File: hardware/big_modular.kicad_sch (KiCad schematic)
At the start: 0 parts

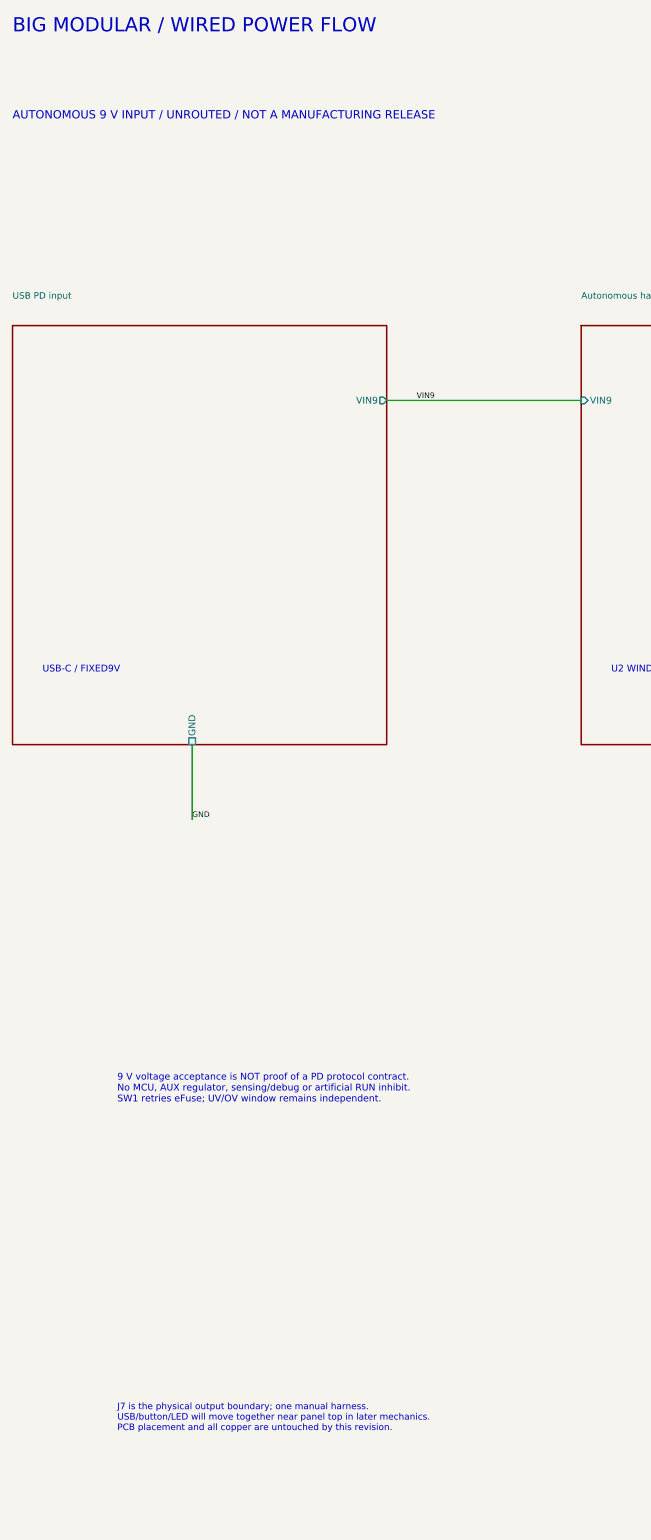
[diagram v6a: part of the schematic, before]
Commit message: Move USB, retry button and power LED to top; synchronize 64 V1 footprints without routing
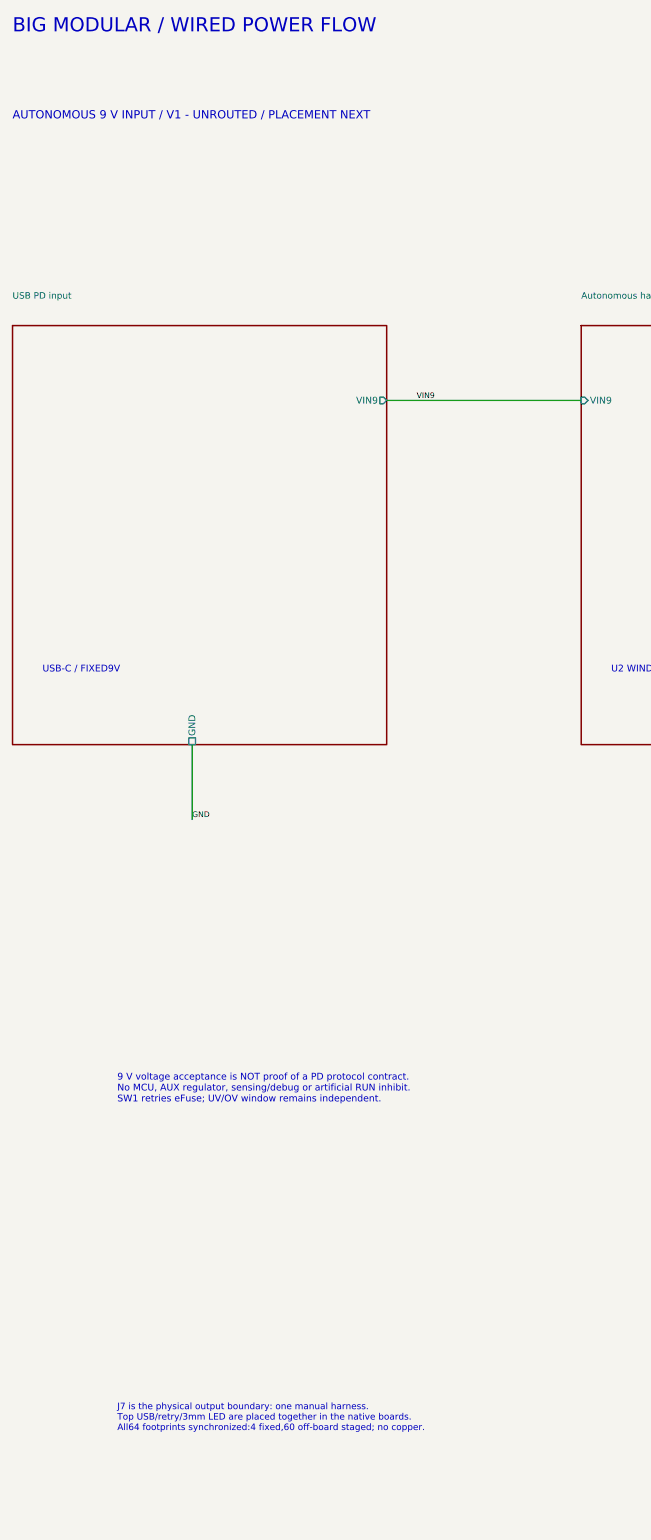
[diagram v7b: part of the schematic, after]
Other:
- note added: "AUTONOMOUS 9 V INPUT / V1 - UNROUTED / PLACEMENT NEXT"
- note added: "J7 is the physical output boundary: one manual harness. Top USB/retry/3mm LED are placed together in the native boards. All64 footprints synchronized:4 fixed,60 off-board staged; no copper."
- note removed: "AUTONOMOUS 9 V INPUT / UNROUTED / NOT A MANUFACTURING RELEASE"
- note removed: "J7 is the physical output boundary; one manual harness. USB/button/LED will move together near panel top in later mechanics. PCB placement and all copper are untouched by this revision."
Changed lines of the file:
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@@
-(kicad_sch (version 20250114) (generator "eeschema") (paper "User" 430 345)
-(title_block (title "Big Modular - V1 electrical hierarchy") (rev "V1 routing preparation") (company "Big Modular") (comment 1 "UNROUTED V1 / NOT A MANUFACTURING RELEASE"))
-(text "BIG MODULAR / WIRED POWER FLOW" (at 20.32 17.78 0) (effects (font (size 2.4 2.4)) (justify left)))
-(text "AUTONOMOUS 9 V INPUT / UNROUTED / NOT A MANUFACTURING RELEASE" (at 20.32 33.02 0) (effects (font (size 1.4 1.4)) (justify left)))
-(sheet (at 20.32 68.58) (size 63.5 71.12) (stroke (width 0.254) (type default)) (fill (color 0 0 0 0))
-(property "Sheetname" "USB PD input" (at 20.32 63.5 0) (effects (font (size 1.1 1.1)) (justify left)))
-(property "Sheetfile" "01_input_protection.kicad_sch" (at 20.32 144.78 0) (effects (font (size .85 .85)) hide))
-(pin "VIN9" output (at 83.82 81.28 0) (effects (font (size 1.15 1.15)) (justify right)))
-(pin "GND" passive (at 50.8 139.7 270) (effects (font (size 1.15 1.15)) (justify left)))
-(instances (project "big_modular" (path "/d567704c-57ad-5df1-b183-cadb01fd8972" (page "2")))) )
-(sheet (at 116.84 68.58) (size 63.5 71.12) (stroke (width 0.254) (type default)) (fill (color 0 0 0 0))
-(property "Sheetname" "Autonomous hardware window and retry" (at 116.84 63.5 0) (effects (font (size 1.1 1.1)) (justify left)))
-(property "Sheetfile" "02_hardgate.kicad_sch" (at 116.84 144.78 0) (effects (font (size .85 .85)) hide))
-(pin "VIN9" input (at 116.84 81.28 180) (effects (font (size 1.15 1.15)) (justify left)))
-(pin "VPROT" output (at 180.34 81.28 0) (effects (font (size 1.15 1.15)) (justify right)))
-(pin "GND" passive (at 147.32 139.7 270) (effects (font (size 1.15 1.15)) (justify left)))
-(instances (project "big_modular" (path "/d567704c-57ad-5df1-b183-cadb01fd8972" (page "3")))) )
-(sheet (at 213.36 68.58) (size 63.5 71.12) (stroke (width 0.254) (type default)) (fill (color 0 0 0 0))
-(property "Sheetname" "Independent buck converters" (at 213.36 63.5 0) (effects (font (size 1.1 1.1)) (justify left)))
-(property "Sheetfile" "03_bucks.kicad_sch" (at 213.36 144.78 0) (effects (font (size .85 .85)) hide))
-(pin "VPROT" input (at 213.36 81.28 180) (effects (font (size 1.15 1.15)) (justify left)))
-(pin "MID" output (at 276.86 81.28 0) (effects (font (size 1.15 1.15)) (justify right)))
-(pin "P5" output (at 276.86 111.76 0) (effects (font (size 1.15 1.15)) (justify right)))
-(pin "GND" passive (at 243.84 139.7 270) (effects (font (size 1.15 1.15)) (justify left)))
-(instances (project "big_modular" (path "/d567704c-57ad-5df1-b183-cadb01fd8972" (page "4")))) )
-(sheet (at 309.88 68.58) (size 76.2 71.12) (stroke (width 0.254) (type default)) (fill (color 0 0 0 0))
-(property "Sheetname" "Direct bipolar rails" (at 309.88 63.5 0) (effects (font (size 1.1 1.1)) (justify left)))
-(property "Sheetfile" "04_bipolar.kicad_sch" (at 309.88 144.78 0) (effects (font (size .85 .85)) hide))
-(pin "MID" input (at 309.88 81.28 180) (effects (font (size 1.15 1.15)) (justify left)))
-(pin "P12" output (at 330.2 139.7 270) (effects (font (size 1.15 1.15)) (justify left)))
-(pin "N12" output (at 360.68 139.7 270) (effects (font (size 1.15 1.15)) (justify left)))
-(pin "GND" passive (at 309.88 127.0 180) (effects (font (size 1.15 1.15)) (justify left)))
-(instances (project "big_modular" (path "/d567704c-57ad-5df1-b183-cadb01fd8972" (page "5")))) )
-(sheet (at 309.88 198.12) (size 76.2 71.12) (stroke (width 0.254) (type default)) (fill (color 0 0 0 0))
-(property "Sheetname" "Board output and power LED" (at 309.88 180.34 0) (effects (font (size 1.1 1.1)) (justify left)))
-(property "Sheetfile" "07_output_rails.kicad_sch" (at 309.88 274.32 0) (effects (font (size .85 .85)) hide))
-(pin "P12" input (at 330.2 198.12 90) (effects (font (size 1.15 1.15)) (justify right)))
-(pin "N12" input (at 360.68 198.12 90) (effects (font (size 1.15 1.15)) (justify right)))
-(pin "P5" input (at 309.88 208.28 180) (effects (font (size 1.15 1.15)) (justify left)))
-(pin "GND" passive (at 335.28 269.24 270) (effects (font (size 1.15 1.15)) (justify left)))
-(instances (project "big_modular" (path "/d567704c-57ad-5df1-b183-cadb01fd8972" (page "6")))) )
-(text "USB-C / FIXED9V" (at 25.4 127.0 0) (effects (font (size 1.15 1.15)) (justify left)))
-(text "U2 WINDOW / SW1 RETRY" (at 121.92 127.0 0) (effects (font (size 1.15 1.15)) (justify left)))
-(text "U3 MID / U5 +5V" (at 218.44 127.0 0) (effects (font (size 1.15 1.15)) (justify left)))
-(text "U4 / +/-12V" (at 314.96 127.0 0) (effects (font (size 1.15 1.15)) (justify left)))
-(text "J7 / D10 P5 LED" (at 314.96 256.54 0) (effects (font (size 1.15 1.15)) (justify left)))
-(label "GND" (at 50.8 152.4 0) (effects (font (size 0.95 0.95)) (justify left bottom)))
-(label "GND" (at 147.32 152.4 0) (effects (font (size 0.95 0.95)) (justify left bottom)))
-(label "GND" (at 243.84 152.4 0) (effects (font (size 0.95 0.95)) (justify left bottom)))
-(label "GND" (at 302.26 127.0 0) (effects (font (size 0.95 0.95)) (justify left bottom)))
-(label "GND" (at 335.28 281.94 0) (effects (font (size 0.95 0.95)) (justify left bottom)))
-(label "VIN9" (at 88.9 81.28 0) (effects (font (size 0.95 0.95)) (justify left bottom)))
-(label "VPROT" (at 185.42 81.28 0) (effects (font (size 0.95 0.95)) (justify left bottom)))
-(label "MID" (at 281.94 81.28 0) (effects (font (size 0.95 0.95)) (justify left bottom)))
-(label "P5" (at 281.94 111.76 0) (effects (font (size 0.95 0.95)) (justify left bottom)))
-(label "P12" (at 330.2 165.1 90) (effects (font (size 0.95 0.95)) (justify left bottom)))
-(label "N12" (at 360.68 165.1 90) (effects (font (size 0.95 0.95)) (justify left bottom)))
-(text "9 V voltage acceptance is NOT proof of a PD protocol contract.\nNo MCU, AUX regulator, sensing/debug or artificial RUN inhibit.\nSW1 retries eFuse; UV/OV window remains independent." (at 38.1 198.12 0) (effects (font (size 1.15 1.15)) (justify left)))
-(text "J7 is the physical output boundary; one manual harness.\nUSB/button/LED will move together near panel top in later mechanics.\nPCB placement and all copper are untouched by this revision." (at 38.1 254.0 0) (effects (font (size 1.1 1.1)) (justify left)))
-(wire (pts (xy 50.8 139.7) (xy 50.8 152.4)) (stroke (width 0) (type default)))
-(wire (pts (xy 147.32 139.7) (xy 147.32 152.4)) (stroke (width 0) (type default)))
-(wire (pts (xy 243.84 139.7) (xy 243.84 152.4)) (stroke (width 0) (type default)))
-(wire (pts (xy 302.26 127.0) (xy 309.88 127.0)) (stroke (width 0) (type default)))
-(wire (pts (xy 335.28 269.24) (xy 335.28 281.94)) (stroke (width 0) (type default)))
-(wire (pts (xy 276.86 81.28) (xy 281.94 81.28)) (stroke (width 0) (type default)))
-(wire (pts (xy 281.94 81.28) (xy 309.88 81.28)) (stroke (width 0) (type default)))
-(wire (pts (xy 360.68 139.7) (xy 360.68 165.1)) (stroke (width 0) (type default)))
-(wire (pts (xy 360.68 165.1) (xy 360.68 198.12)) (stroke (width 0) (type default)))
-(wire (pts (xy 330.2 139.7) (xy 330.2 165.1)) (stroke (width 0) (type default)))
-(wire (pts (xy 330.2 165.1) (xy 330.2 198.12)) (stroke (width 0) (type default)))
-(wire (pts (xy 276.86 111.76) (xy 281.94 111.76)) (stroke (width 0) (type default)))
-(wire (pts (xy 281.94 111.76) (xy 294.64 111.76)) (stroke (width 0) (type default)))
-(wire (pts (xy 294.64 111.76) (xy 294.64 208.28)) (stroke (width 0) (type default)))
-(wire (pts (xy 294.64 208.28) (xy 309.88 208.28)) (stroke (width 0) (type default)))
-(wire (pts (xy 83.82 81.28) (xy 88.9 81.28)) (stroke (width 0) (type default)))
-(wire (pts (xy 88.9 81.28) (xy 116.84 81.28)) (stroke (width 0) (type default)))
-(wire (pts (xy 180.34 81.28) (xy 185.42 81.28)) (stroke (width 0) (type default)))
-(wire (pts (xy 185.42 81.28) (xy 213.36 81.28)) (stroke (width 0) (type default)))
-(sheet_instances (path "/" (page "1")))
-(embedded_fonts no))

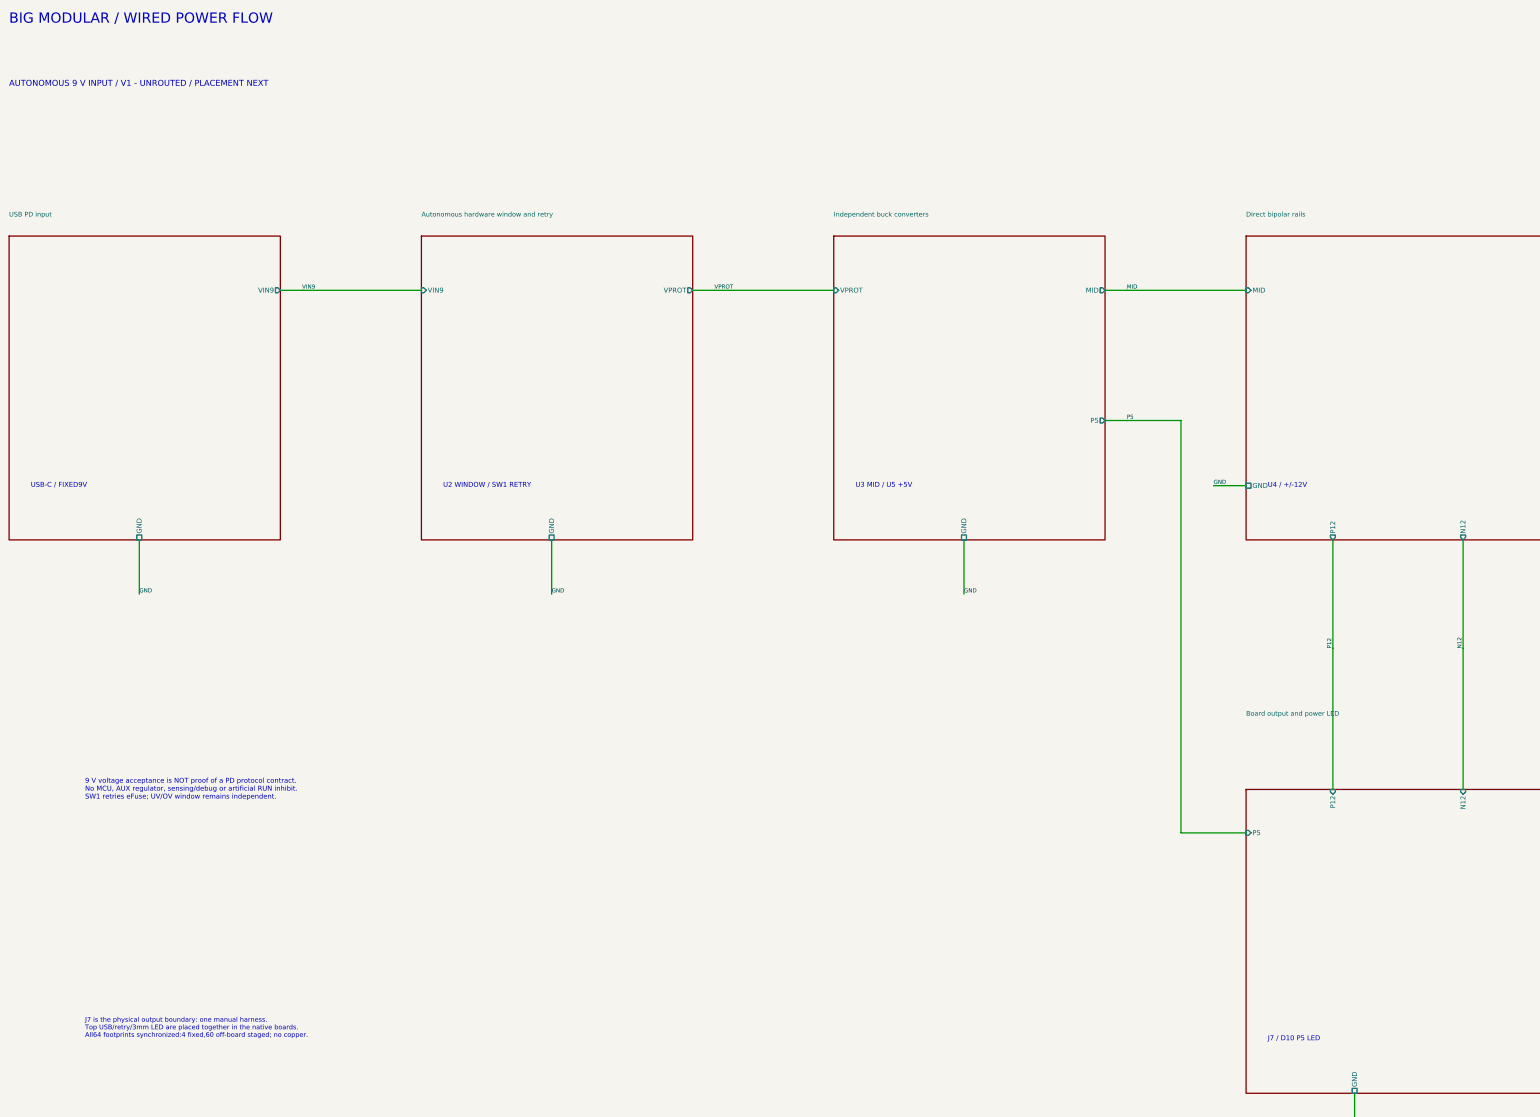
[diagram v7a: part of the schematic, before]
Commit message: Complete four-layer routing, adopt proven HRO USB-C and release checked fabrication files
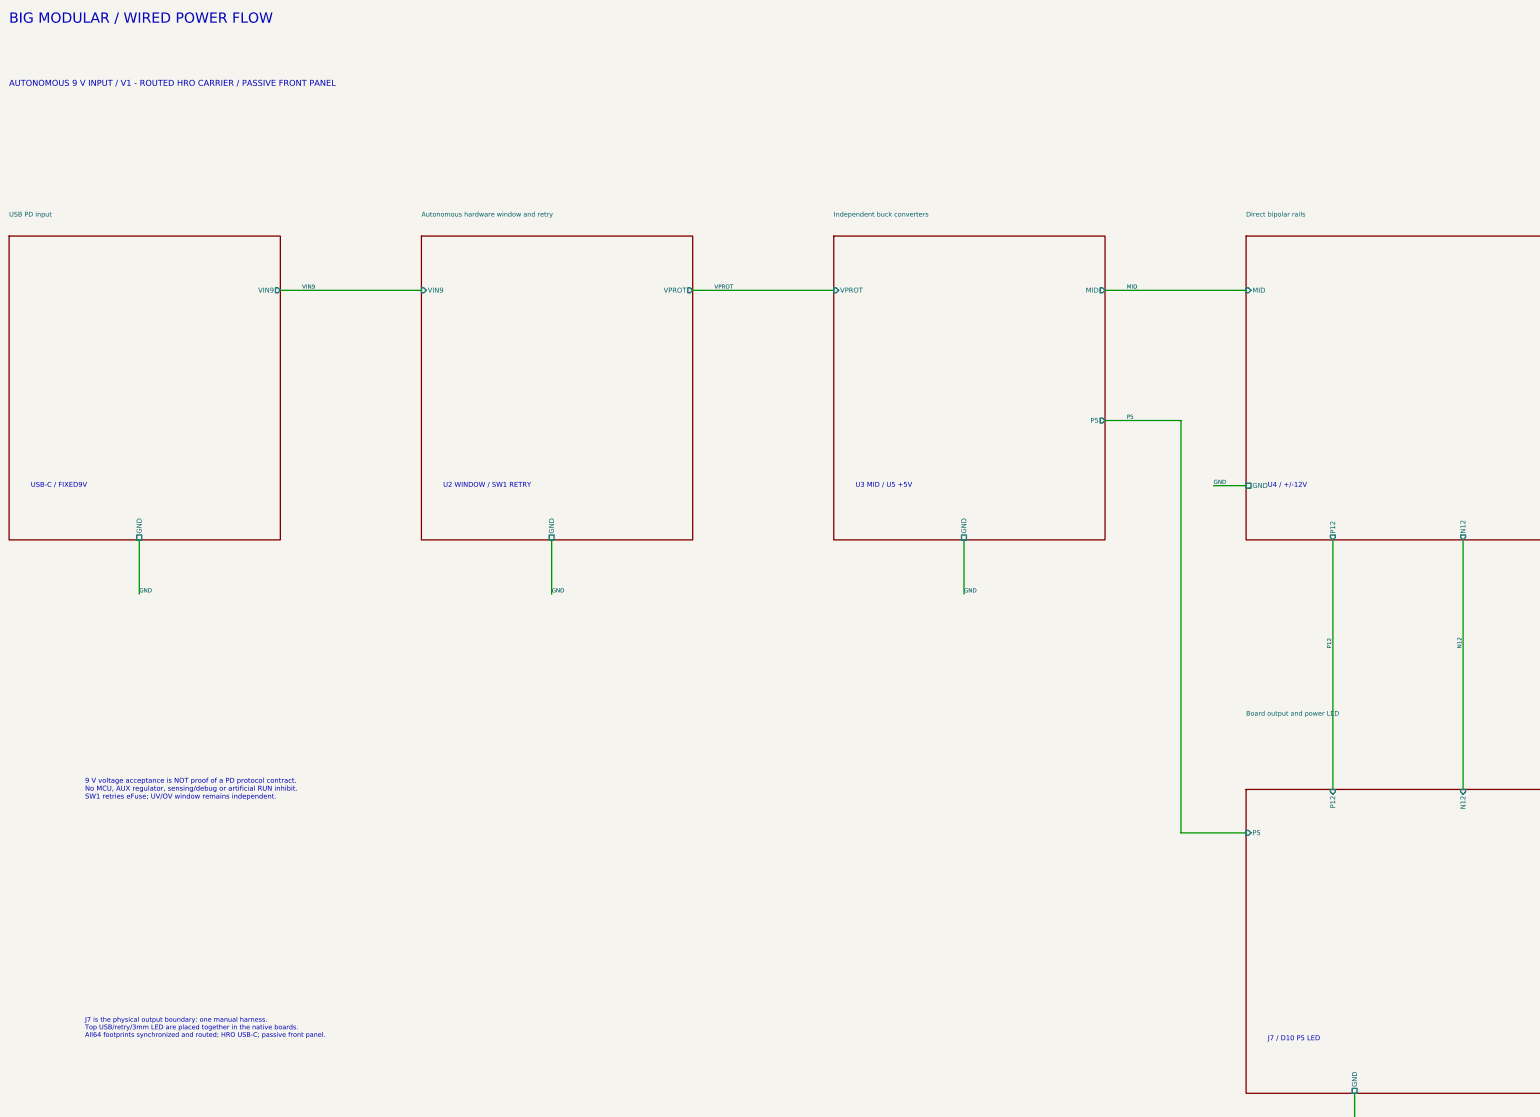
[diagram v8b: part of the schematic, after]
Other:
- note added: "AUTONOMOUS 9 V INPUT / V1 - ROUTED HRO CARRIER / PASSIVE FRONT PANEL"
- note added: "J7 is the physical output boundary: one manual harness. Top USB/retry/3mm LED are placed together in the native boards. All64 footprints synchronized and routed; HRO USB-C; passive front panel."
- note removed: "AUTONOMOUS 9 V INPUT / V1 - UNROUTED / PLACEMENT NEXT"
- note removed: "J7 is the physical output boundary: one manual harness. Top USB/retry/3mm LED are placed together in the native boards. All64 footprints synchronized:4 fixed,60 off-board staged; no copper."
